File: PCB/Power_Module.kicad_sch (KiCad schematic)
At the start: 36 parts, among them Q1 AO3401A, Q2 LBSS84LT1G, Q3 LBSS84LT1G, U1 TP4056, U2 XC6206P, U3 OP07

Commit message: literally all the footprints
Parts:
- removed C5: 0.1u, symbol Device:C_Small
- BT1: footprint (none) -> Justins:18650_Holder_SMD
- C1, C4: footprint (none) -> JLC:CAP-SMD_L3.2-W1.6-RD-C7171
- C2: value 10u -> 1u; footprint (none) -> JLC:C0402_NEW
- C3: value 22u -> 1u; footprint (none) -> JLC:C0402_NEW
- D1, D2: footprint (none) -> JLC_Diodes:SOD-323_L1.8-W1.3-LS2.5-RD
- D3: footprint (none) -> JLC_Diodes:LL-34_L3.5-W1.5-RD
- J? (x2): footprint (none) -> Connector_PinSocket_2.54mm:PinSocket_1x02_P2.54mm_Vertical
- LED1: footprint (none) -> JLC_Diodes:LED0603-RD
- LED2: footprint (none) -> JLC_Diodes:LED0805-R-RD
- Q2, Q3: footprint (none) -> JLC_Mosfet:SOT-23_L2.9-W1.3-P1.90-LS2.4-BR
- R1, R10, R11, R12, R2, R3, R4, R5, R6, R7, R8, R9: footprint (none) -> Resistor_SMD:R_0805_2012Metric
- R13: renamed from R51; footprint (none) -> Resistor_SMD:R_0805_2012Metric
- R14: renamed from R13; footprint (none) -> Resistor_SMD:R_0805_2012Metric
- R15: renamed from R14; footprint (none) -> Resistor_SMD:R_0805_2012Metric
- R16: renamed from R15; footprint (none) -> Resistor_SMD:R_0805_2012Metric
- R17: renamed from R16; footprint (none) -> Resistor_SMD:R_0805_2012Metric
- U3: footprint (none) -> JLC_Opamp:SOIC-8_L4.9-W3.9-P1.27-LS6.0-BL

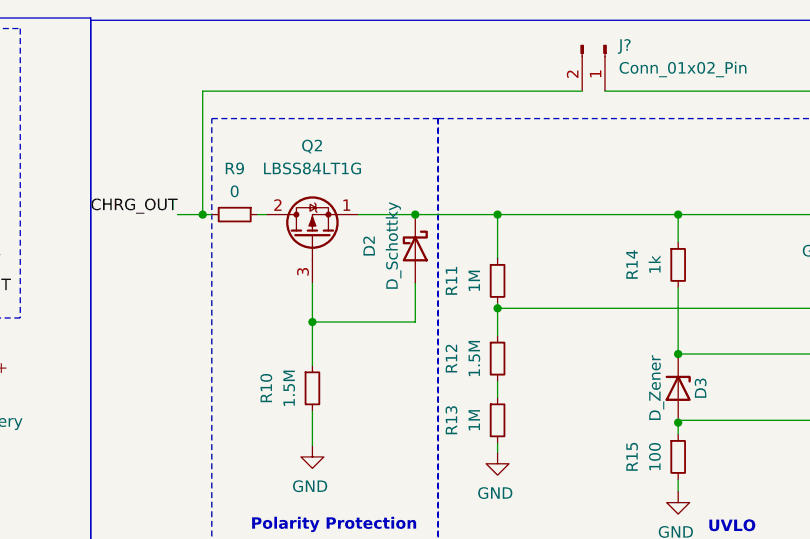
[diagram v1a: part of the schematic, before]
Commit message: Fixed via issues on PCB
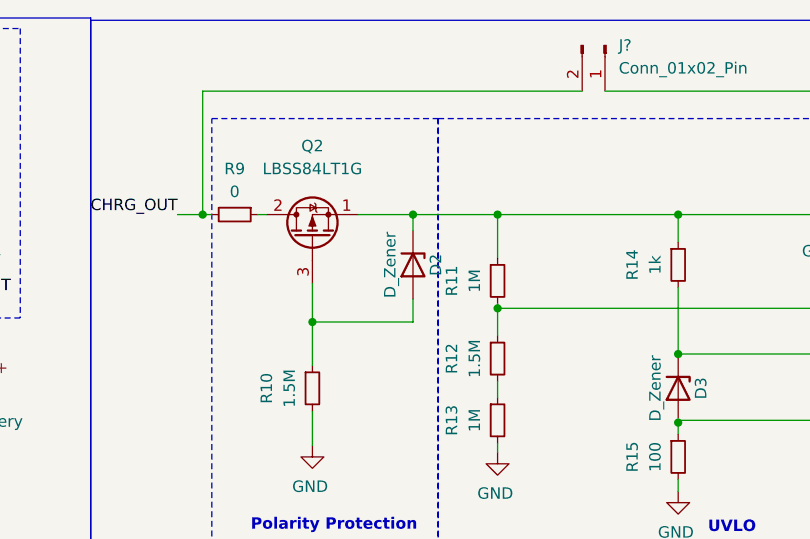
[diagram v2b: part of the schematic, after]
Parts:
- removed D2: D_Schottky, JLC_Diodes:SOD-323_L1.8-W1.3-LS2.5-RD, symbol Device:D_Schottky
- added D2: D_Zener, JLC_Diodes:LL-34_L3.5-W1.5-RD, symbol Device:D_Zener
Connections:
- net at Q2.1 (S), Q3.1 (S), R11.1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: now also D2.1 (K)
- net at Q2.3 (G), R10.1: now also D2.2 (A)
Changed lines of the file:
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@@
     (comment 1 "Author: Adrian Mc Intosh")
   )
-  (junction (at 195.834 34.544) (diameter 0) (color 0 0 0 0)
-  )
   (junction (at 172.212 34.544) (diameter 0) (color 0 0 0 0)
   )
@@
   )
   (junction (at 44.704 52.324) (diameter 0) (color 0 0 0 0)
+  )
+  (junction (at 195.58 34.544) (diameter 0) (color 0 0 0 0)
   )
   (junction (at 276.098 34.544) (diameter 0) (color 0 0 0 0)
@@
     (stroke (width 0) (type default))
   )
+  (wire (pts (xy 195.58 36.322) (xy 195.58 34.544))
+    (stroke (width 0) (type default))
+  )
   (wire (pts (xy 137.414 32.004) (xy 137.414 33.274))
     (stroke (width 0) (type default))
@@
     (stroke (width 0) (type default))
   )
+  (wire (pts (xy 195.58 34.544) (xy 204.978 34.544))
+    (stroke (width 0) (type default))
+  )
   (wire (pts (xy 172.212 20.828) (xy 214.376 20.828))
     (stroke (width 0) (type default))
@@
     (stroke (width 0) (type default))
   )
-  (wire (pts (xy 195.834 34.544) (xy 204.978 34.544))
+  (wire (pts (xy 189.484 34.544) (xy 195.58 34.544))
     (stroke (width 0) (type default))
   )
@@
     (stroke (width 0) (type default))
   )
-  (wire (pts (xy 189.484 34.544) (xy 195.834 34.544))
-    (stroke (width 0) (type default))
-  )
   (wire (pts (xy 82.804 48.514) (xy 91.694 48.514))
     (stroke (width 0) (type default))
@@
     (stroke (width 0) (type default))
   )
-  (wire (pts (xy 195.834 46.482) (xy 195.834 42.164))
+  (wire (pts (xy 195.58 46.482) (xy 195.58 43.942))
     (stroke (width 0) (type default))
   )
@@
     (stroke (width 0) (type default))
   )
-  (wire (pts (xy 184.404 46.482) (xy 195.834 46.482))
+  (wire (pts (xy 184.404 46.482) (xy 195.58 46.482))
     (stroke (width 0) (type default))
   )
@@
     )
   )
-  (symbol (lib_id "Device:D_Schottky") (at 195.834 38.354 270) (unit 1)
-    (in_bom yes) (on_board yes) (dnp no) (fields_autoplaced)
-    (property "Reference" "D2" (at 190.754 38.0365 0)
-      (effects (font (size 1.27 1.27)))
-    )
-    (property "Value" "D_Schottky" (at 193.294 38.0365 0)
-      (effects (font (size 1.27 1.27)))
-    )
-    (property "Footprint" "JLC_Diodes:SOD-323_L1.8-W1.3-LS2.5-RD" (at 195.834 38.354 0)
-      (effects (font (size 1.27 1.27)) hide)
-    )
-    (property "Datasheet" "~" (at 195.834 38.354 0)
-      (effects (font (size 1.27 1.27)) hide)
-    )
-    (pin "1")
-    (pin "2")
-    (instances
-      (project "HAT"
-        (path "/40f36b19-a08c-43e7-88a6-ec8387939712/13666b47-888a-4bed-b522-fee751a1c440"
-          (reference "D2") (unit 1)
-        )
-      )
-      (project "Power_Module"
-        (path "/9518a89f-42c8-4f0b-818e-9ddc6754f3b2"
-          (reference "D?") (unit 1)
-        )
-      )
-    )
-  )
   (symbol (lib_id "Device:C_Small") (at 56.007 123.952 0) (unit 1)
     (in_bom yes) (on_board yes) (dnp no) (fields_autoplaced)
@@
         )
       )
+    )
+  )
+  (symbol (lib_id "Device:D_Zener") (at 195.58 40.132 270) (unit 1)
+    (in_bom yes) (on_board yes) (dnp no)
+    (property "Reference" "D2" (at 198.12 40.132 0)
+      (effects (font (size 1.27 1.27)))
+    )
+    (property "Value" "D_Zener" (at 193.04 40.132 0)
+      (effects (font (size 1.27 1.27)))
+    )
+    (property "Footprint" "JLC_Diodes:LL-34_L3.5-W1.5-RD" (at 195.58 40.132 0)
+      (effects (font (size 1.27 1.27)) hide)
+    )
+    (property "Datasheet" "~" (at 195.58 40.132 0)
+      (effects (font (size 1.27 1.27)) hide)
+    )
+    (pin "1")
+    (pin "2")
+    (instances
+      (project "HAT"
+        (path "/40f36b19-a08c-43e7-88a6-ec8387939712/13666b47-888a-4bed-b522-fee751a1c440"
+          (reference "D2") (unit 1)
+        )
+      )

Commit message: Pins not Sockets
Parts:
- J? (x2): footprint Connector_PinSocket_2.54mm:PinSocket_1x02_P2.54mm_Vertical -> Connector_PinHeader_2.54mm:PinHeader_1x02_P2.54mm_Vertical
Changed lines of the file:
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@@
       (effects (font (size 1.27 1.27)) (justify left))
     )
-    (property "Footprint" "Connector_PinSocket_2.54mm:PinSocket_1x02_P2.54mm_Vertical" (at 74.8284 92.3544 0)
+    (property "Footprint" "Connector_PinHeader_2.54mm:PinHeader_1x02_P2.54mm_Vertical" (at 74.8284 92.3544 0)
       (effects (font (size 1.27 1.27)) hide)
     )
@@
       (effects (font (size 1.27 1.27)) (justify left))
     )
-    (property "Footprint" "Connector_PinSocket_2.54mm:PinSocket_1x02_P2.54mm_Vertical" (at 216.916 15.748 0)
-      (effects (font (size 1.27 1.27)) hide)
-    )
+    (property "Footprint" "Connector_PinHeader_2.54mm:PinHeader_1x02_P2.54mm_Vertical" (at 216.916 15.748 0)
+      (effects (font (size 1.27 1.27)) hide)
+    )

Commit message: Final Fixes
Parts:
- added D4: D_Schottky, JLC_Diodes:SOD-323_L1.8-W1.3-LS2.5-RD, symbol Device:D_Schottky
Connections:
- net V_BAT+: now also D4.2 (A); no longer Q1.2 (S)
- new net: D4.1 (K), Q1.2 (S)
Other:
- moved on the sheet: R6, R8
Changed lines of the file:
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@@
   (junction (at 172.212 34.544) (diameter 0) (color 0 0 0 0)
   )
-  (junction (at 109.474 32.004) (diameter 0) (color 0 0 0 0)
-  )
   (junction (at 129.794 32.004) (diameter 0) (color 0 0 0 0)
   )
@@
   (junction (at 118.1608 113.792) (diameter 0) (color 0 0 0 0)
   )
+  (junction (at 109.22 32.004) (diameter 0) (color 0 0 0 0)
+  )
   (junction (at 137.414 43.434) (diameter 0) (color 0 0 0 0)
   )
@@
   (junction (at 49.022 42.164) (diameter 0) (color 0 0 0 0)
   )
-  (junction (at 120.904 43.434) (diameter 0) (color 0 0 0 0)
+  (junction (at 114.808 43.434) (diameter 0) (color 0 0 0 0)
   )
   (junction (at 225.044 34.544) (diameter 0) (color 0 0 0 0)
@@
     (stroke (width 0) (type default))
   )
-  (wire (pts (xy 59.944 32.004) (xy 109.474 32.004))
+  (wire (pts (xy 59.944 32.004) (xy 109.22 32.004))
     (stroke (width 0) (type default))
   )
@@
     (stroke (width 0) (type default))
   )
-  (wire (pts (xy 120.904 43.434) (xy 124.714 43.434))
-    (stroke (width 0) (type default))
-  )
   (wire (pts (xy 44.704 42.164) (xy 44.704 52.324))
     (stroke (width 0) (type default))
@@
     (stroke (width 0) (type default))
   )
+  (wire (pts (xy 109.22 32.004) (xy 129.794 32.004))
+    (stroke (width 0) (type default))
+  )
   (wire (pts (xy 118.872 113.792) (xy 118.1608 113.792))
     (stroke (width 0) (type default))
@@
     (stroke (width 0) (type default))
   )
-  (wire (pts (xy 118.364 43.434) (xy 120.904 43.434))
+  (wire (pts (xy 112.268 43.434) (xy 114.808 43.434))
     (stroke (width 0) (type default))
   )
@@
     (stroke (width 0) (type default))
   )
+  (wire (pts (xy 124.206 43.434) (xy 124.714 43.434))
+    (stroke (width 0) (type default))
+  )
   (wire (pts (xy 118.1608 113.792) (xy 118.1608 101.4984))
     (stroke (width 0) (type default))
@@
     (stroke (width 0) (type default))
   )
-  (wire (pts (xy 109.474 32.004) (xy 129.794 32.004))
-    (stroke (width 0) (type default))
-  )
   (wire (pts (xy 29.464 42.164) (xy 32.004 42.164))
     (stroke (width 0) (type default))
@@
     (stroke (width 0) (type default))
   )
-  (wire (pts (xy 109.474 32.004) (xy 109.474 45.974))
+  (wire (pts (xy 114.808 43.434) (xy 116.586 43.434))
     (stroke (width 0) (type default))
   )
@@
     (stroke (width 0) (type default))
   )
+  (wire (pts (xy 109.22 32.004) (xy 109.22 33.02))
+    (stroke (width 0) (type default))
+  )
   (wire (pts (xy 56.007 120.142) (xy 70.612 120.142))
     (stroke (width 0) (type default))
@@
     (stroke (width 0) (type default))
   )
-  (wire (pts (xy 120.904 47.244) (xy 120.904 43.434))
+  (wire (pts (xy 114.808 47.244) (xy 114.808 43.434))
     (stroke (width 0) (type default))
   )
@@
     (stroke (width 0) (type default))
   )
-  (wire (pts (xy 101.219 43.434) (xy 113.284 43.434))
+  (wire (pts (xy 101.219 43.434) (xy 107.188 43.434))
     (stroke (width 0) (type default))
   )
@@
     (effects (font (size 1.27 1.27)) (justify left))
   )
-  (hierarchical_label "V_BAT+" (shape output) (at 120.904 47.244 270) (fields_autoplaced)
+  (hierarchical_label "V_BAT+" (shape output) (at 114.808 47.244 270) (fields_autoplaced)
     (effects (font (size 1.27 1.27)) (justify right))
   )
@@
         (path "/e63e39d7-6ac0-4ffd-8aa3-1841a4541b55"
           (reference "R?") (unit 1)
+        )
+      )
+    )
+  )
+  (symbol (lib_id "Device:D_Schottky") (at 120.396 43.434 180) (unit 1)
+    (in_bom yes) (on_board yes) (dnp no) (fields_autoplaced)
+    (property "Reference" "D4" (at 120.7135 37.846 0)
+      (effects (font (size 1.27 1.27)))
+    )
+    (property "Value" "D_Schottky" (at 120.7135 40.386 0)
+      (effects (font (size 1.27 1.27)))
+    )
+    (property "Footprint" "JLC_Diodes:SOD-323_L1.8-W1.3-LS2.5-RD" (at 120.396 43.434 0)
+      (effects (font (size 1.27 1.27)) hide)
+    )
+    (property "Datasheet" "~" (at 120.396 43.434 0)
+      (effects (font (size 1.27 1.27)) hide)
+    )
+    (pin "1")
+    (pin "2")
+    (instances
+      (project "HAT"
+        (path "/40f36b19-a08c-43e7-88a6-ec8387939712/13666b47-888a-4bed-b522-fee751a1c440"
+          (reference "D4") (unit 1)
+        )
+      )
+      (project "Power_Module"
+        (path "/9518a89f-42c8-4f0b-818e-9ddc6754f3b2"
+          (reference "D?") (unit 1)
         )
       )
@@
     )
   )
-  (symbol (lib_id "Device:R_Small") (at 115.824 43.434 270) (unit 1)
-    (in_bom yes) (on_board yes) (dnp no)
-    (property "Reference" "R8" (at 115.824 38.354 90)
-      (effects (font (size 1.27 1.27)))
-    )
-    (property "Value" "0" (at 115.824 40.894 90)
-      (effects (font (size 1.27 1.27)))
-    )
-    (property "Footprint" "Resistor_SMD:R_0805_2012Metric" (at 115.824 43.434 0)
-      (effects (font (size 1.27 1.27)) hide)
-    )
-    (property "Datasheet" "~" (at 115.824 43.434 0)
+  (symbol (lib_id "Device:R_Small") (at 109.728 43.434 270) (unit 1)
+    (in_bom yes) (on_board yes) (dnp no)
+    (property "Reference" "R8" (at 109.474 47.498 90)
+      (effects (font (size 1.27 1.27)))
+    )
+    (property "Value" "0" (at 109.474 45.72 90)
+      (effects (font (size 1.27 1.27)))
+    )
+    (property "Footprint" "Resistor_SMD:R_0805_2012Metric" (at 109.728 43.434 0)
+      (effects (font (size 1.27 1.27)) hide)
+    )
+    (property "Datasheet" "~" (at 109.728 43.434 0)
       (effects (font (size 1.27 1.27)) hide)
     )
@@
     )
   )
-  (symbol (lib_id "power:GND") (at 109.474 51.054 0) (unit 1)
-    (in_bom yes) (on_board yes) (dnp no) (fields_autoplaced)
-    (property "Reference" "#PWR010" (at 109.474 57.404 0)
-      (effects (font (size 1.27 1.27)) hide)
-    )
-    (property "Value" "GND" (at 109.474 55.499 0)
-      (effects (font (size 1.27 1.27)))
-    )
-    (property "Footprint" "" (at 109.474 51.054 0)
-      (effects (font (size 1.27 1.27)) hide)
-    )
-    (property "Datasheet" "" (at 109.474 51.054 0)
+  (symbol (lib_id "power:GND") (at 109.22 38.1 0) (unit 1)
+    (in_bom yes) (on_board yes) (dnp no)
+    (property "Reference" "#PWR010" (at 109.22 44.45 0)
+      (effects (font (size 1.27 1.27)) hide)
+    )
+    (property "Value" "GND" (at 106.426 38.354 0)
+      (effects (font (size 1.27 1.27)))
+    )
+    (property "Footprint" "" (at 109.22 38.1 0)
+      (effects (font (size 1.27 1.27)) hide)
+    )
+    (property "Datasheet" "" (at 109.22 38.1 0)
       (effects (font (size 1.27 1.27)) hide)
     )
@@
     )
   )
-  (symbol (lib_id "Device:R_Small") (at 109.474 48.514 180) (unit 1)
-    (in_bom yes) (on_board yes) (dnp no)
-    (property "Reference" "R6" (at 113.2332 50.9524 0)
-      (effects (font (size 1.27 1.27)))
-    )
-    (property "Value" "10k" (at 113.2332 48.4124 0)
-      (effects (font (size 1.27 1.27)))
-    )
-    (property "Footprint" "Resistor_SMD:R_0805_2012Metric" (at 109.474 48.514 0)
-      (effects (font (size 1.27 1.27)) hide)
-    )
-    (property "Datasheet" "~" (at 109.474 48.514 0)
-      (effects (font (size 1.27 1.27)) hide)
-    )
+  (symbol (lib_id "Device:R_Small") (at 109.22 35.56 180) (unit 1)
+    (in_bom yes) (on_board yes) (dnp no)
+    (property "Reference" "R6" (at 112.9792 37.9984 0)
+      (effects (font (size 1.27 1.27)))
+    )
+    (property "Value" "10k" (at 112.9792 35.4584 0)
+      (effects (font (size 1.27 1.27)))
+    )
+    (property "Footprint" "Resistor_SMD:R_0805_2012Metric" (at 109.22 35.56 0)
+      (effects (font (size 1.27 1.27)) hide)
+    )
+    (property "Datasheet" "~" (at 109.22 35.56 0)
+      (effects (font (size 1.27 1.27)) hide)
+    )
